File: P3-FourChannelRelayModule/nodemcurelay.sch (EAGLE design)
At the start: 22 parts, among them IC1 7812T, K1 CQ1-12V, K2 CQ1-12V, K3 CQ1-12V, K4 CQ1-12V, T1 2N2222, T2 2N2222, T3 2N2222, T4 2N2222

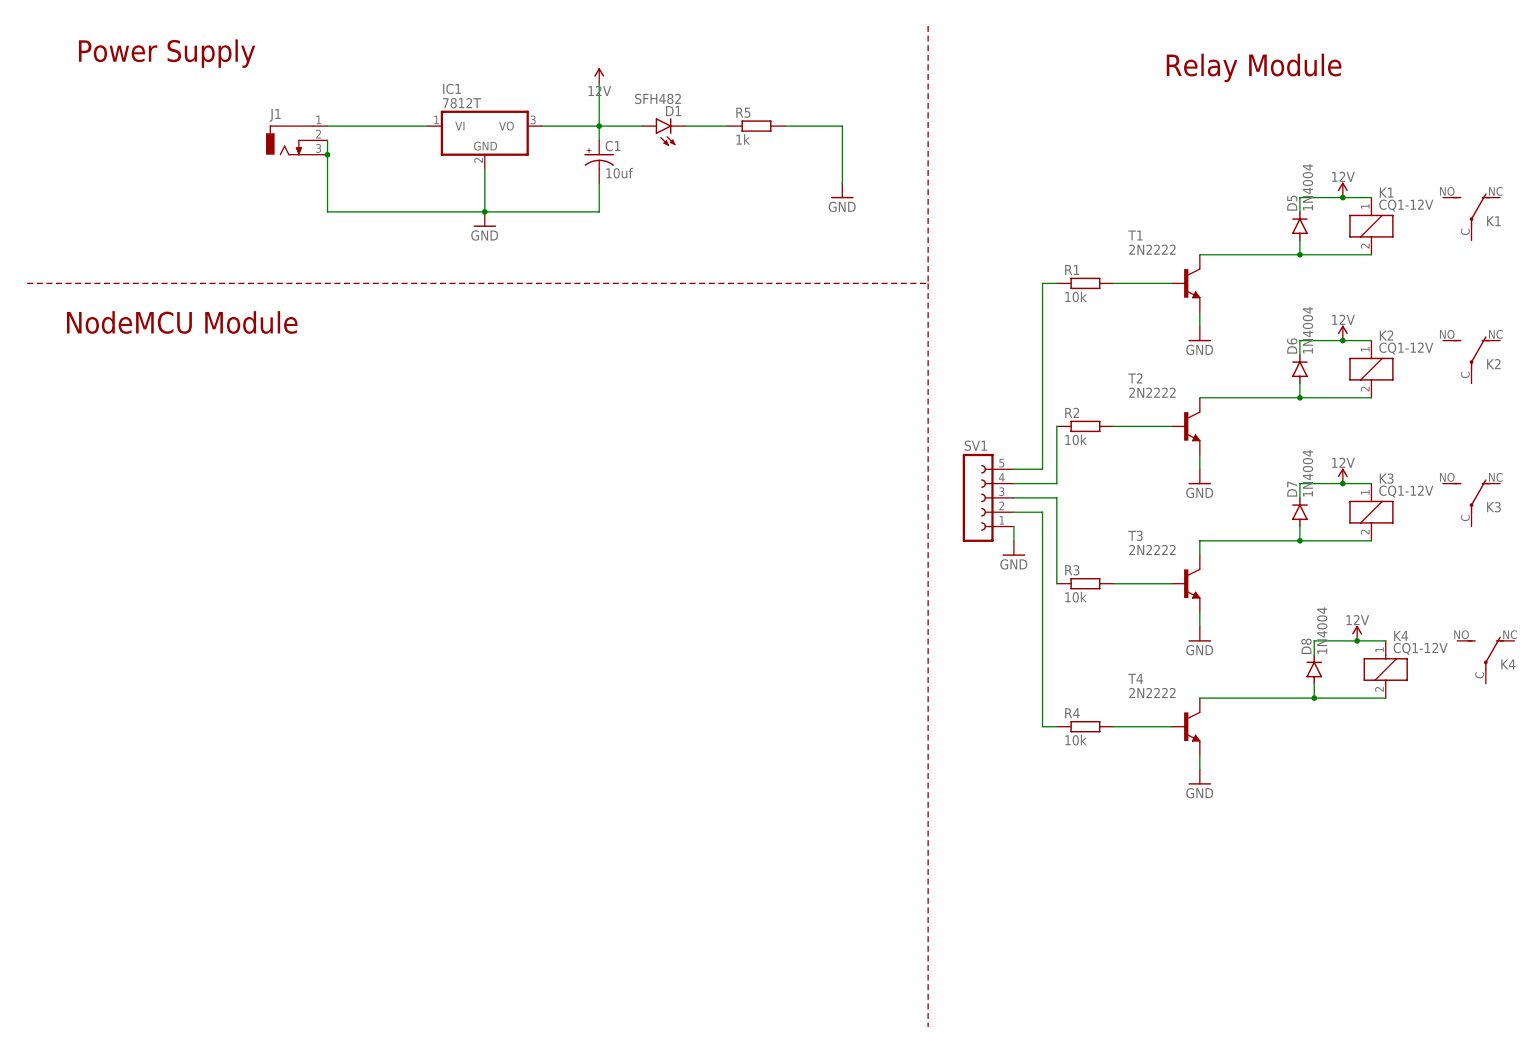
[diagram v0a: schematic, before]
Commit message: Updated Relay Boards
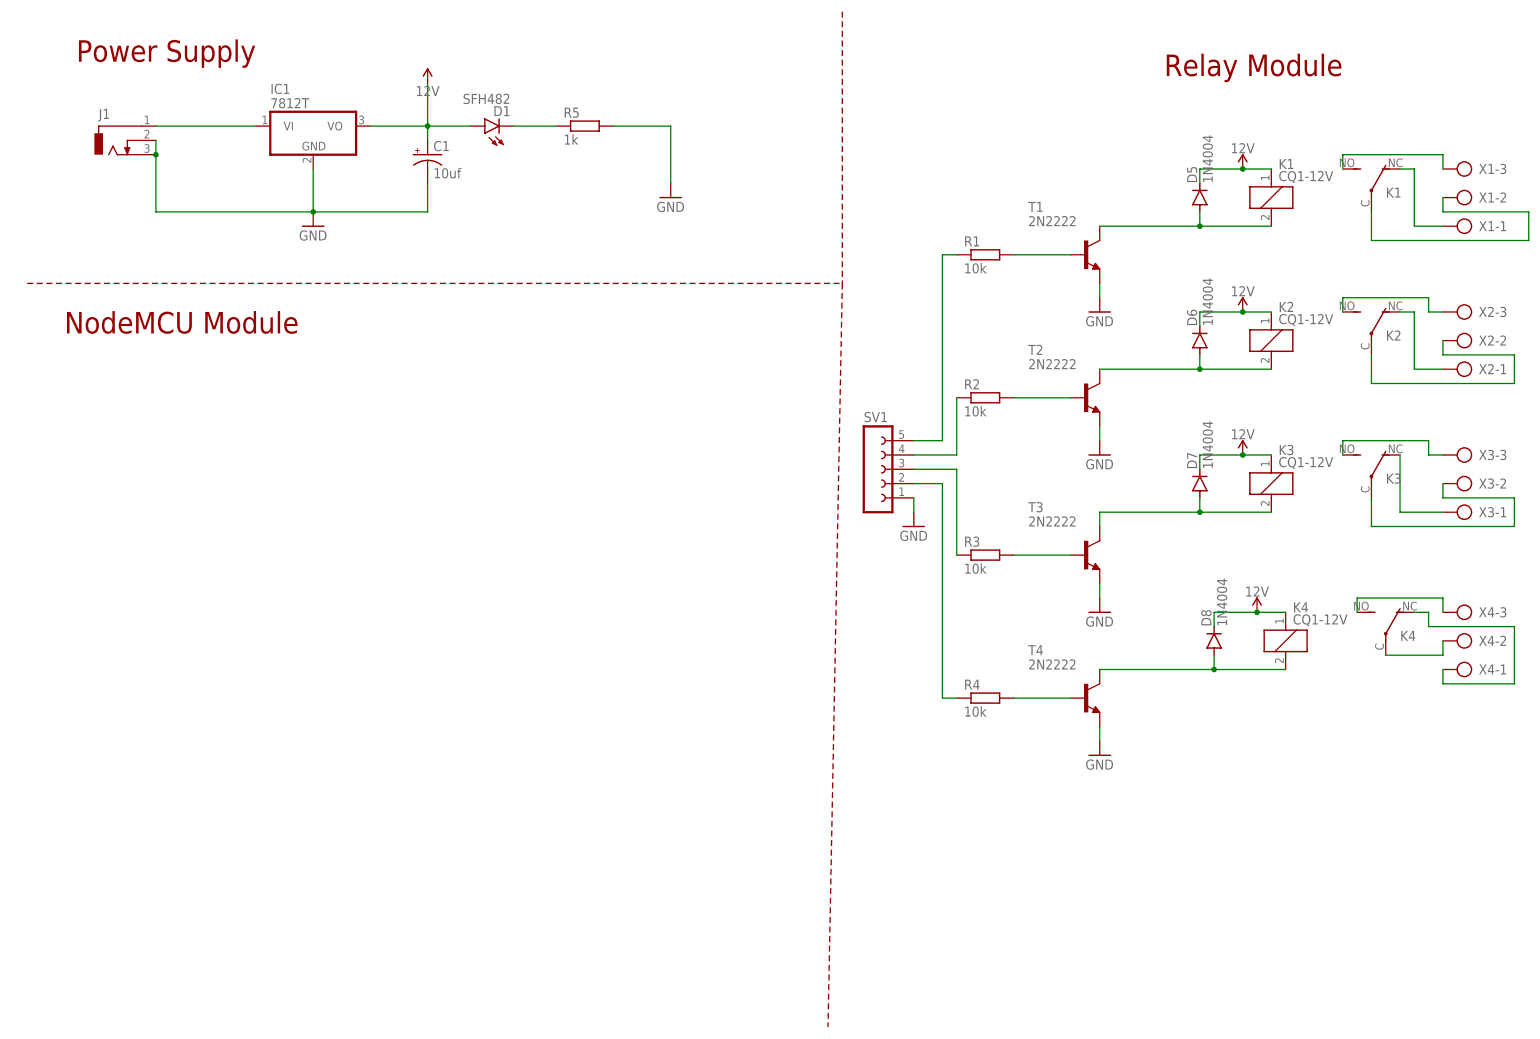
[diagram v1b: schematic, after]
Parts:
- added X1, X2, X3, X4: (no value), con-ptr500:AK300/3
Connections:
- new net N$11: K12.O, X1-1.KL
- new net N$17: K12.P, X1-2.KL
- new net N$18: K22.O, X2-1.KL
- new net N$19: K22.P, X2-2.KL
- new net N$20: K22.S, X2-3.KL
- new net N$21: K32.S, X3-3.KL
- new net N$22: K32.O, X3-1.KL
- new net N$23: K32.P, X3-2.KL
- new net N$24: K42.S, X4-3.KL
- new net N$25: K42.P, X4-2.KL
- new net N$26: K42.O, X4-1.KL
- new net N$7: K12.S, X1-3.KL
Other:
- moved on the sheet: C1, D1, D5, D6, D7, D8, IC1, J1, K1, K2, K3, K4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
